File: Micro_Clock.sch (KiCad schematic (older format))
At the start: 25 parts, among them IC1 ATMEGA328-P, P1 CONN_01X04, P2 CONN_02X03, Q3 2N7002, Q4 2N7002, Q5 2N7002, SW1 SW_PUSH, SW2 SW_PUSH, U3 DS1307+, U4 MAX31855KASA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

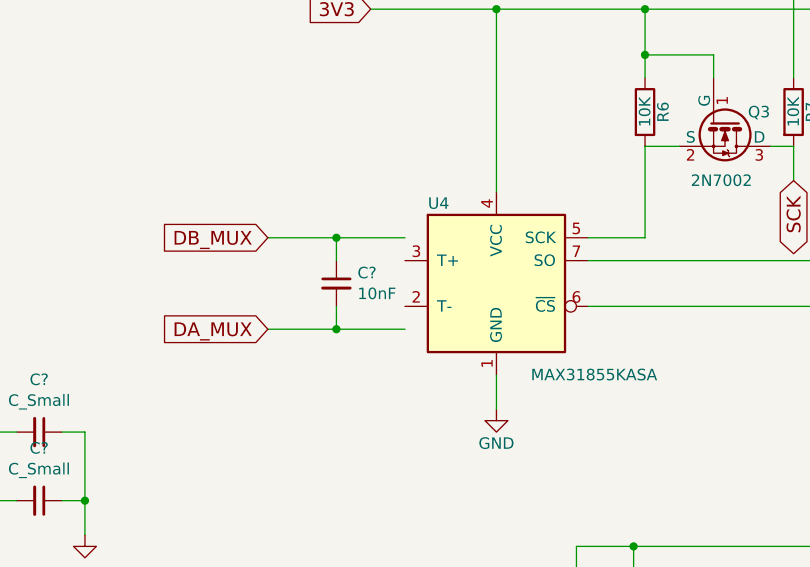
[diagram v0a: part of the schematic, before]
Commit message: Reconnect TC amplifier
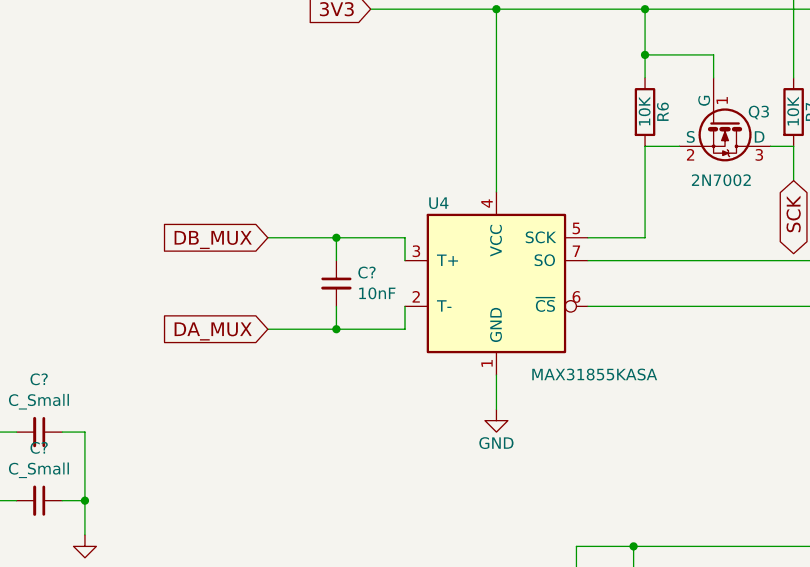
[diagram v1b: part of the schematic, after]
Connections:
- wire segments 107 -> 109
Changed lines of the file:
@@
 	4900 3800 5500 3800
 Connection ~ 2100 3000
+Wire Wire Line
+	7200 2650 7200 2750
+Wire Wire Line
+	7200 2950 7200 3050
 $EndSCHEMATC
